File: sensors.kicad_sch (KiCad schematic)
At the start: 0 parts

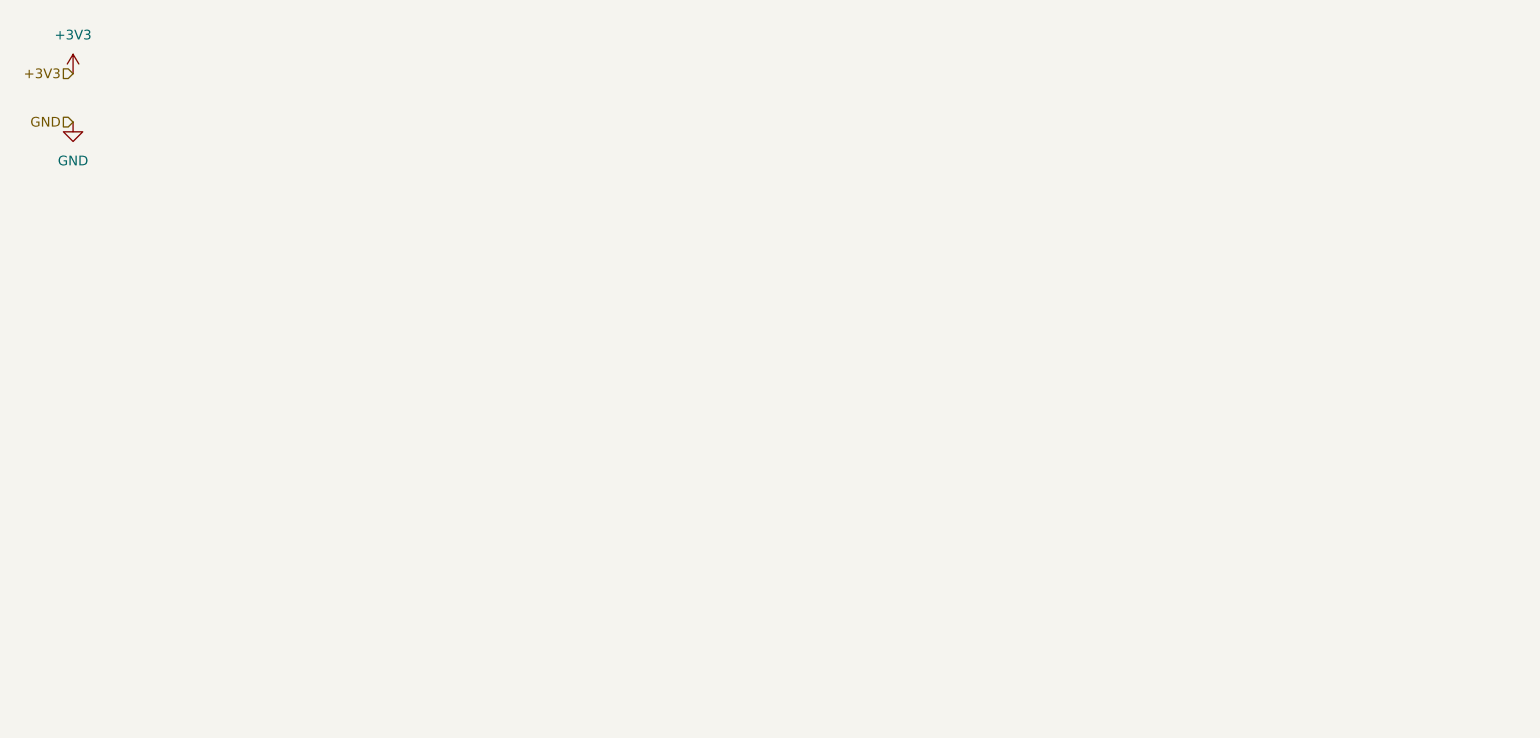
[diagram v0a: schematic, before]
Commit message: Merged sensors topsheet
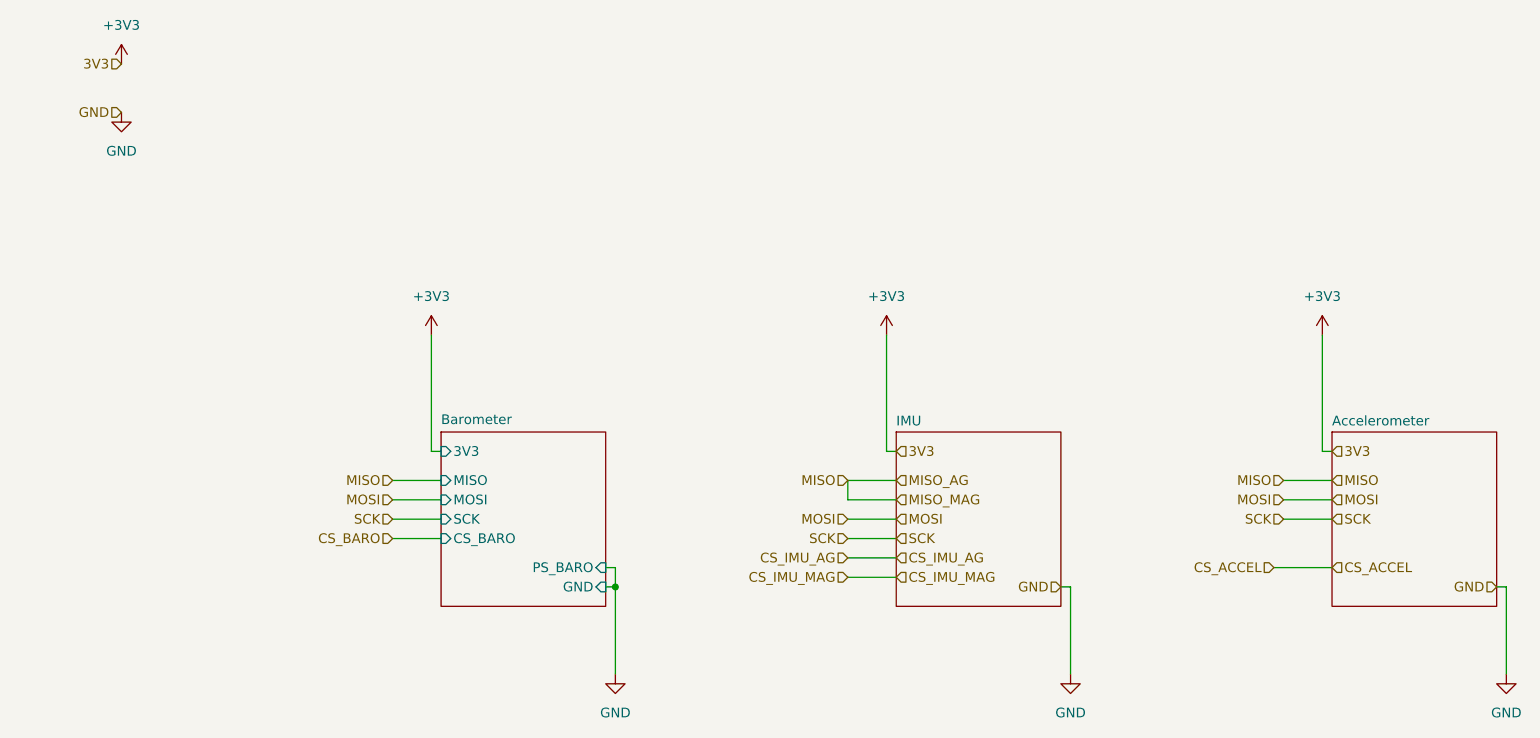
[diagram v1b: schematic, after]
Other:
- added sheet Accelerometer (accelerometer.kicad_sch)
- added sheet Barometer (barometer.kicad_sch)
- added sheet IMU (imu.kicad_sch)
